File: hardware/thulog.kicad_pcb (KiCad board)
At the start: 2 copper layers, 16 parts, among them IC1 ATTINY2313A-S, K1 DHT, P1 ISP, P2 USB, X1 QUARTZCMS4

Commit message: modified quartz
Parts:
- X1: footprint CONN3_SMD -> SM2512
- moved X1 29.0 mm to (50.8, 31.8), turned to 180 degrees
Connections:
- X1 pad 3: N-000002 -> (no net)
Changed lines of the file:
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@@
 (kicad_pcb (version 3) (host pcbnew "(2013-07-07 BZR 4022)-stable")
   (general
-    (links 34)
-    (no_connects 34)
+    (links 33)
+    (no_connects 33)
     (area 0 0 0 0)
     (thickness 1.6)
@@
     (mod_text_size 1 1)
     (mod_text_width 0.15)
-    (pad_size 1.5 1.5)
-    (pad_drill 0.6)
+    (pad_size 1.99898 2.99974)
+    (pad_drill 0)
     (pad_to_mask_clearance 0)
     (aux_axis_origin 0 0)
@@
     )
   )
-  (module CONN3_SMD (layer F.Cu)
-    (at 25.4 17.78)
-    (attr smd)
-    (fp_text reference X1 (at 0 -0.381) (layer F.SilkS)
-      (effects (font (size 1.016 0.762) (thickness 0.1524)))
-    )
-    (fp_text value QUARTZCMS4 (at 0 -1.524) (layer F.SilkS)
-      (effects (font (size 0.762 0.762) (thickness 0.1524)))
-    )
-    (fp_line (start 2.667 1.3335) (end 2.667 0.381) (layer F.SilkS) (width 0.127))
-    (fp_line (start 2.667 0.381) (end -2.667 0.381) (layer F.SilkS) (width 0.127))
-    (fp_line (start -2.667 0.381) (end -2.667 1.3335) (layer F.SilkS) (width 0.127))
-    (fp_line (start 0 -2.794) (end 2.794 -2.794) (layer F.SilkS) (width 0.127))
-    (fp_line (start 2.794 -2.794) (end 2.794 -2.032) (layer F.SilkS) (width 0.127))
-    (fp_line (start 2.794 -2.032) (end 4.826 -2.032) (layer F.SilkS) (width 0.127))
-    (fp_line (start 4.826 -2.032) (end 4.826 1.3335) (layer F.SilkS) (width 0.127))
-    (fp_line (start 4.826 1.3335) (end -4.826 1.3335) (layer F.SilkS) (width 0.127))
-    (fp_line (start -4.826 1.3335) (end -4.826 -2.032) (layer F.SilkS) (width 0.127))
-    (fp_line (start -4.826 -2.032) (end -2.794 -2.032) (layer F.SilkS) (width 0.127))
-    (fp_line (start -2.794 -2.032) (end -2.794 -2.794) (layer F.SilkS) (width 0.127))
-    (fp_line (start -2.794 -2.794) (end 0 -2.794) (layer F.SilkS) (width 0.127))
-    (pad 3 smd rect (at 1.27 -3.429) (size 0.8128 1.778)
-      (layers F.Cu F.Paste F.Mask)
-      (net 6 N-000002)
-    )
-    (pad 2 smd rect (at 0 -3.429) (size 0.8128 1.778)
-      (layers F.Cu F.Paste F.Mask)
-    )
-    (pad 1 smd rect (at -1.27 -3.429) (size 0.8128 1.778)
-      (layers F.Cu F.Paste F.Mask)
-      (net 2 N-000001)
-    )
-    (pad "" smd rect (at 3.81 -0.4445) (size 2.032 3.048)
-      (layers F.Cu F.Paste F.Mask)
-    )
-    (pad "" smd rect (at -3.81 -0.4445) (size 2.032 3.048)
-      (layers F.Cu F.Paste F.Mask)
-    )
-    (model smd/conn3_smd.wrl
-      (at (xyz 0 0 0))
-      (scale (xyz 0.4 0.4 0.4))
-      (rotate (xyz 0 0 0))
-    )
-  )
   (module SM0805 (layer F.Cu)
     (at 67.31 45.72)
@@
       (rotate (xyz 0 0 0))
     )
+  )
+  (module SM2512 (layer F.Cu)
+    (at 50.8 31.75 180)
+    (tags "CMS SM")
+    (attr smd)
+    (fp_text reference X1 (at -0.8001 0 270) (layer F.SilkS)
+      (effects (font (size 0.889 0.762) (thickness 0.127)))
+    )
+    (fp_text value QUARTZCMS4 (at 0.89916 0 270) (layer F.SilkS)
+      (effects (font (size 0.889 0.762) (thickness 0.127)))
+    )
+    (fp_line (start -3.99956 -2.10058) (end -3.99956 2.10058) (layer F.SilkS) (width 0.14986))
+    (fp_text user + (at -4.59994 2.30124 180) (layer F.SilkS)
+      (effects (font (size 0.7 0.7) (thickness 0.15)))
+    )
+    (fp_line (start -4.30022 -2.10058) (end -4.30022 2.10058) (layer F.SilkS) (width 0.14986))
+    (fp_line (start 4.30022 -2.10058) (end 4.30022 2.10058) (layer F.SilkS) (width 0.14986))
+    (fp_line (start 1.99644 2.10566) (end 4.28244 2.10566) (layer F.SilkS) (width 0.14986))
+    (fp_line (start 4.28244 -2.10566) (end 1.99644 -2.10566) (layer F.SilkS) (width 0.14986))
+    (fp_line (start -1.99898 -2.10566) (end -4.28498 -2.10566) (layer F.SilkS) (width 0.14986))
+    (fp_line (start -4.28244 2.10566) (end -1.99644 2.10566) (layer F.SilkS) (width 0.14986))
+    (pad 1 smd rect (at -2.99974 0 180) (size 1.99898 2.99974)
+      (layers F.Cu F.Paste F.Mask)
+      (net 2 N-000001)
+    )
+    (pad 3 smd rect (at 2.99974 0 180) (size 1.99898 2.99974)
+      (layers F.Cu F.Paste F.Mask)
+    )
+    (model smd\chip_smd_pol_wide.wrl
+      (at (xyz 0 0 0))
+      (scale (xyz 0.35 0.35 0.35))
+      (rotate (xyz 0 0 0))
+    )

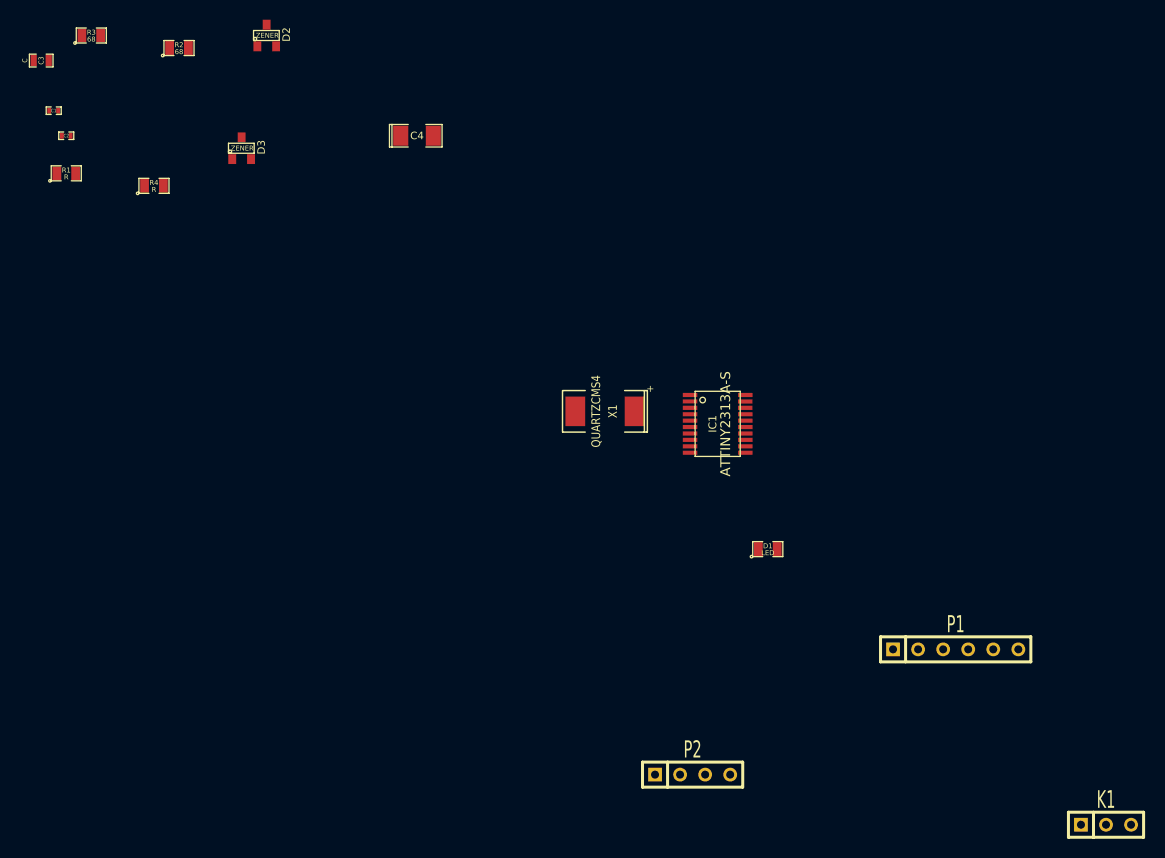
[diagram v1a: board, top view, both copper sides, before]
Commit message: drawing the pcb
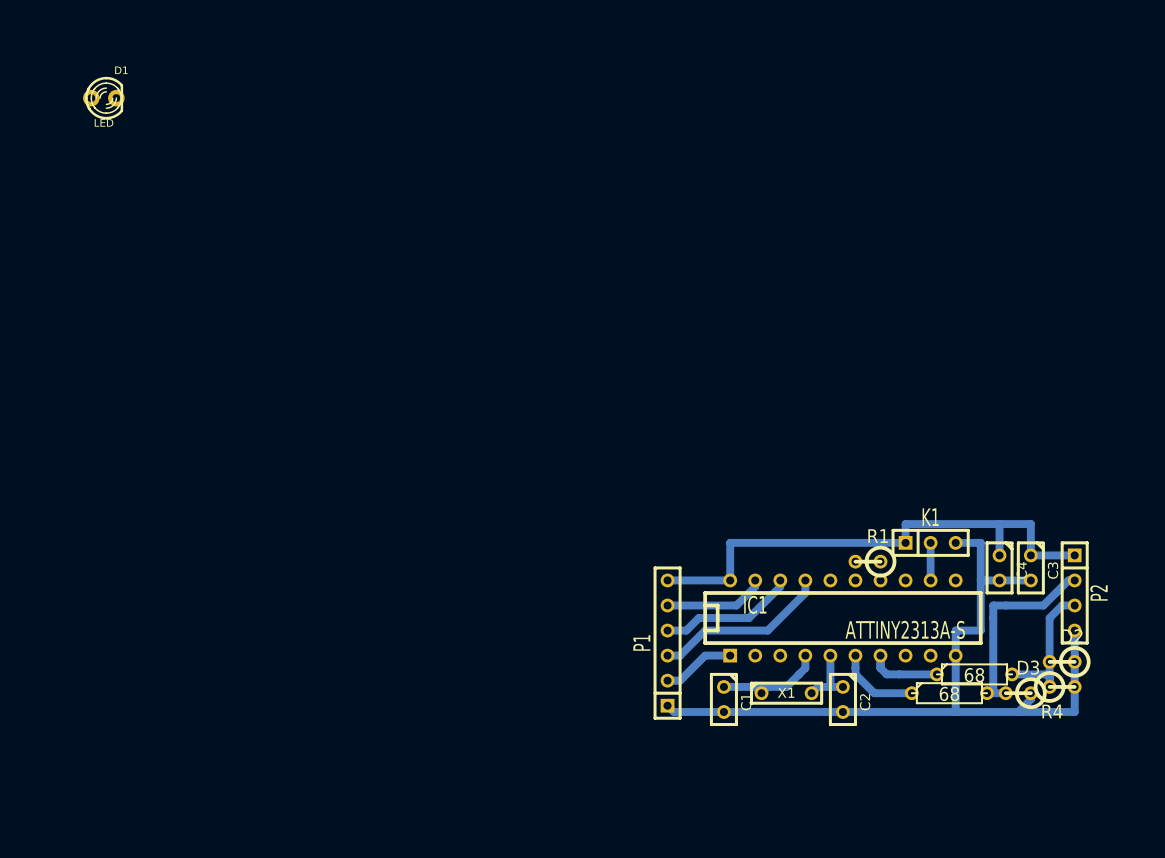
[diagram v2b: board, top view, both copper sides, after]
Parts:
- C1, C2: footprint SM0402_c -> C1
- C3: footprint SM0603_Capa -> C1
- C4: footprint SM1206POL -> C1
- D1: footprint SM0805 -> LED-3MM
- D2, D3: footprint SOT23 -> R1
- IC1: footprint tssop-20 -> DIP-20__300
- R1, R4: footprint SM0805 -> R1
- R2, R3: footprint SM0805 -> R3
- X1: footprint SM2512 -> C2
- moved C3 112.7 mm to (94.0, 47.6), turned to 270 degrees
- moved R3 110.5 mm to (88.3, 58.4)
- moved R4 105.2 mm to (97.2, 59.7)
- moved D2 102.6 mm to (97.2, 57.1), turned to 180 degrees
- moved R2 101.9 mm to (85.7, 60.3)
- moved C2 97.3 mm to (74.9, 61.0), turned to 270 degrees
- moved D3 96.2 mm to (92.7, 60.3), turned to 180 degrees
- moved C1 90.4 mm to (62.9, 61.0), turned to 270 degrees
- moved R1 90.3 mm to (77.5, 47.0), turned to 180 degrees
- moved D1 81.4 mm to (0.00, 0.00)
- moved C4 73.5 mm to (90.8, 47.6), turned to 270 degrees
- moved P2 42.9 mm to (98.4, 50.2), turned to 270 degrees
- moved X1 34.0 mm to (69.2, 60.3), turned to 0 degrees
- moved K1 33.7 mm to (83.8, 45.1)
- moved P1 29.2 mm to (57.1, 55.2), turned to 90 degrees
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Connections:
- C2 pad 1: N-000002 -> N-000009
- IC1 pad 13: (no net) -> N-0000010
- IC1 pad 5: N-000002 -> N-000009
- IC1 pad 8: N-0000023 (its old number) -> (no net)
- P1 pad 1: VCC -> GND
- P1 pad 6: GND -> VCC
- R1 pad 1: N-0000023 (its old number) -> N-0000010
- X1 pad 3: (no net) -> N-000009
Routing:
- net GND: track 0.00 -> 79.5 mm
- net VCC: track 0.00 -> 53.3 mm
- net N-0000022: track 0.00 -> 20.7 mm
- net N-000001: track 0.00 -> 17.9 mm
- net N-0000023: track 0.00 -> 15.1 mm
- net N-000004: track 0.00 -> 13.9 mm
- net N-000008: track 0.00 -> 12.1 mm
- net N-000003: track 0.00 -> 10.3 mm
- net N-0000018: track 0.00 -> 8.52 mm
- net N-0000019: track 0.00 -> 8.41 mm
- net RESET: track 0.00 -> 7.40 mm
- net N-000009: track 0.00 -> 6.61 mm
- net N-000006: track 0.00 -> 3.81 mm
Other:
- net class Default: trace_width 0.254 -> 0.8

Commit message: finished with pcb, ready to be printed
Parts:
- added P3: CONN_2, SIL-2, B.Cu at (132.3, 64.0)
- C1, C2, C3, C4: footprint C1 -> SM0805
- D2, D3, R1, R4: footprint R1 -> SM0805
- IC1: footprint DIP-20__300 -> SO20L
- K1, P1, X1: moved to B.Cu
- P2: value USB -> CONN_2; footprint SIL-4 -> SIL-2; moved to B.Cu
- R2, R3: footprint R3 -> SM0805
- moved D1 125.1 mm to (118.6, 39.9), turned to 220 degrees
- moved C1 71.9 mm to (134.1, 51.1), turned to 0 degrees
- moved P1 70.3 mm to (127.3, 60.7), turned to 180 degrees
- moved X1 64.4 mm to (132.8, 50.3), turned to 90 degrees
- moved C2 60.9 mm to (134.1, 46.7), turned to 0 degrees
- moved R2 53.6 mm to (139.2, 56.6), turned to 270 degrees
- moved IC1 51.1 mm to (125.7, 47.0), turned to 90 degrees
- moved R3 49.0 mm to (136.9, 52.6), turned to 270 degrees
- moved D3 46.1 mm to (138.7, 64.0), turned to 0 degrees
- moved P2 41.4 mm to (138.4, 60.7), turned to 180 degrees
- moved R1 40.1 mm to (117.6, 48.0), turned to 270 degrees
- moved R4 38.9 mm to (135.9, 55.6), turned to 180 degrees
- moved D2 38.7 mm to (135.9, 57.7), turned to 0 degrees
- moved C4 34.4 mm to (120.9, 64.3)
- moved K1 31.1 mm to (108.5, 64.0), turned to 180 degrees
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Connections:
- D1 pad 1: N-0000011 -> N-0000010
- D1 pad 2: GND -> N-000007
- IC1 pad 7: N-0000018 -> (no net)
- IC1 pad 8: (no net) -> N-000008
- P2 pad 1: VCC -> N-0000022
- P2 pad 2: N-0000022 -> N-0000023
- R1 pad 1: N-0000010 -> N-000007
- R1 pad 2: N-0000011 -> GND
- R3 pad 1: N-0000018 -> N-000008
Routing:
- net N-0000017: track 8.41 -> 38.5 mm
- net N-000002: track 3.81 -> 33.7 mm
- net N-000008: track 0.00 -> 26.2 mm
- net N-0000022: track 20.7 -> 6.65 mm
- net GND: track 79.5 -> 91.7 mm
- net N-0000010: track 0.00 -> 10.6 mm
- net N-0000018: track 8.52 -> 0.00 mm
- net N-0000023: track 15.1 -> 7.33 mm
- net N-000007: track 0.00 -> 6.38 mm
- net N-0000013: track 12.1 -> 6.45 mm
- net N-0000014: track 6.61 -> 2.15 mm
- net VCC: track 53.3 -> 55.7 mm
- net N-000006: track 17.9 -> 16.1 mm
- net N-000004: track 10.3 -> 11.1 mm
- net RESET: track 7.40 -> 8.08 mm
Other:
- board outline added: 37.6 x 30.7 mm
- net class Default: trace_width 0.8 -> 0.5

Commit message: adjusted the pbc
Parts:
- moved K1 0.51 mm to (109.0, 64.0)
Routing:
- net VCC: track 55.7 -> 42.2 mm
- net N-000006: track 16.1 -> 19.2 mm
- net N-000005: track 13.6 -> 15.4 mm
- net GND: track 91.7 -> 90.7 mm
- net N-000004: track 11.1 -> 11.7 mm
- net N-000002: track 33.7 -> 33.2 mm
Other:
- board size 37.6 x 30.7 mm -> 37.8 x 30.7 mm

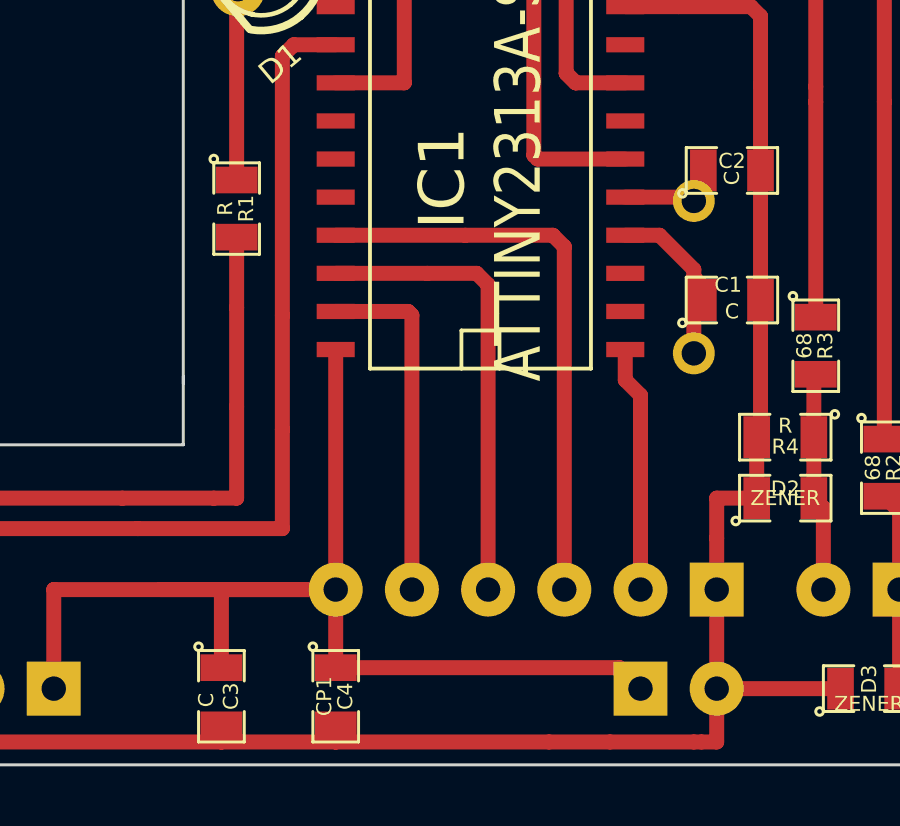
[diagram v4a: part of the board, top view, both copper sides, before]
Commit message: adjusted 0.1uF cap
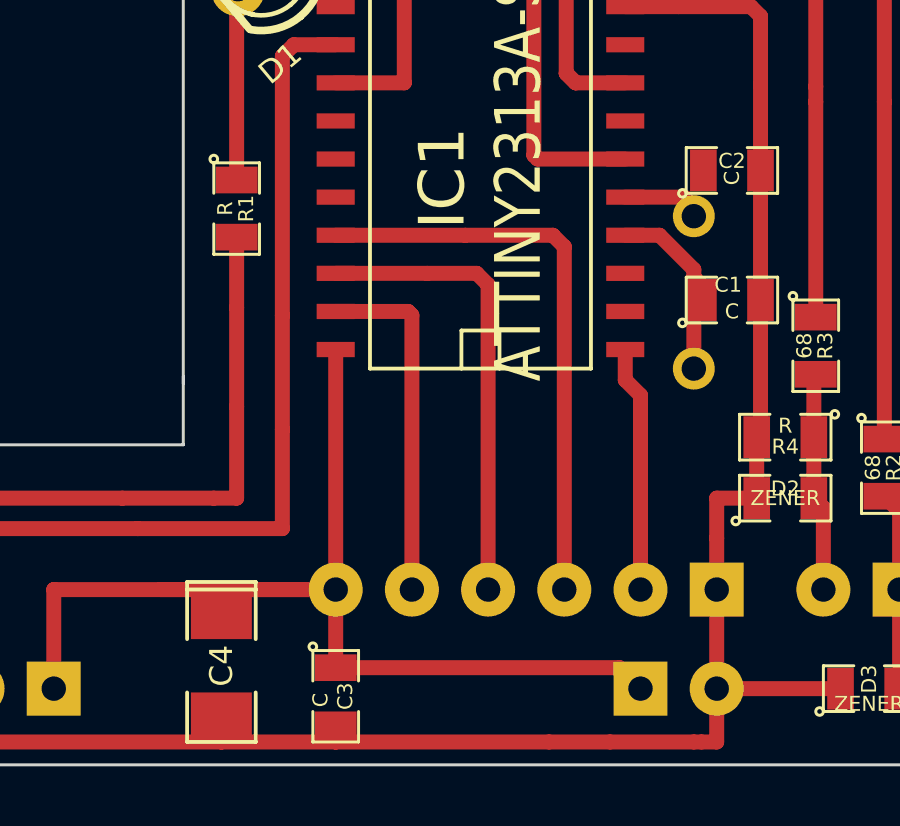
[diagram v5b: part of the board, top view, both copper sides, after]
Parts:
- C4: footprint SM0805 -> SM1206POL
- moved C4 3.94 mm to (117.1, 63.2)
- moved C3 3.81 mm to (120.9, 64.3)
- moved X1 0.51 mm to (132.8, 50.8)
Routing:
- net VCC: track 42.2 -> 40.7 mm
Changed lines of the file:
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@@
     (links 34)
     (no_connects 1)
-    (area 103.078001 35.763999 163.448 76.614)
+    (area 103.327999 35.763999 163.448 67.81927)
     (thickness 1.6)
     (drawings 9)
@@
   )
   (module C2 (layer B.Cu)
-    (at 132.842 50.292 90)
+    (at 132.842 50.8 90)
     (descr "Condensateur = 2 pas")
     (tags C)
@@
   (module SM0805 (layer F.Cu)
     (at 120.904 64.262 270)
-    (attr smd)
-    (fp_text reference C4 (at 0 -0.3175 270) (layer F.SilkS)
-      (effects (font (size 0.50038 0.50038) (thickness 0.10922)))
-    )
-    (fp_text value CP1 (at 0 0.381 270) (layer F.SilkS)
-      (effects (font (size 0.50038 0.50038) (thickness 0.10922)))
-    )
-    (fp_circle (center -1.651 0.762) (end -1.651 0.635) (layer F.SilkS) (width 0.09906))
-    (fp_line (start -0.508 0.762) (end -1.524 0.762) (layer F.SilkS) (width 0.09906))
-    (fp_line (start -1.524 0.762) (end -1.524 -0.762) (layer F.SilkS) (width 0.09906))
-    (fp_line (start -1.524 -0.762) (end -0.508 -0.762) (layer F.SilkS) (width 0.09906))
-    (fp_line (start 0.508 -0.762) (end 1.524 -0.762) (layer F.SilkS) (width 0.09906))
-    (fp_line (start 1.524 -0.762) (end 1.524 0.762) (layer F.SilkS) (width 0.09906))
-    (fp_line (start 1.524 0.762) (end 0.508 0.762) (layer F.SilkS) (width 0.09906))
-    (pad 1 smd rect (at -0.9525 0 270) (size 0.889 1.397)
-      (layers F.Cu F.Paste F.Mask)
-      (net 15 VCC)
-    )
-    (pad 2 smd rect (at 0.9525 0 270) (size 0.889 1.397)
-      (layers F.Cu F.Paste F.Mask)
-      (net 1 GND)
-    )
-    (model smd/chip_cms.wrl
-      (at (xyz 0 0 0))
-      (scale (xyz 0.1 0.1 0.1))
-      (rotate (xyz 0 0 0))
-    )
-  )
-  (module SM0805 (layer F.Cu)
-    (at 117.094 64.262 270)
     (attr smd)
     (fp_text reference C3 (at 0 -0.3175 270) (layer F.SilkS)
@@
     )
   )
-  (gr_line (start 103.632 66.548) (end 103.378 66.548) (angle 90) (layer Edge.Cuts) (width 0.1))
-  (gr_line (start 103.632 55.88) (end 103.632 66.548) (angle 90) (layer Edge.Cuts) (width 0.1))
-  (gr_line (start 115.824 55.88) (end 115.824 53.594) (angle 90) (layer Edge.Cuts) (width 0.1))
-  (gr_line (start 103.632 55.88) (end 115.824 55.88) (angle 90) (layer Edge.Cuts) (width 0.1))
+  (module SM1206POL (layer F.Cu)
+    (at 117.094 63.246 270)
+    (attr smd)
+    (fp_text reference C4 (at 0 0 270) (layer F.SilkS)
+      (effects (font (size 0.762 0.762) (thickness 0.127)))
+    )
+    (fp_text value CP1 (at 0 0 270) (layer F.SilkS) hide
+      (effects (font (size 0.762 0.762) (thickness 0.127)))
+    )
+    (fp_line (start -2.54 -1.143) (end -2.794 -1.143) (layer F.SilkS) (width 0.127))
+    (fp_line (start -2.794 -1.143) (end -2.794 1.143) (layer F.SilkS) (width 0.127))
+    (fp_line (start -2.794 1.143) (end -2.54 1.143) (layer F.SilkS) (width 0.127))
+    (fp_line (start -2.54 -1.143) (end -2.54 1.143) (layer F.SilkS) (width 0.127))
+    (fp_line (start -2.54 1.143) (end -0.889 1.143) (layer F.SilkS) (width 0.127))
+    (fp_line (start 0.889 -1.143) (end 2.54 -1.143) (layer F.SilkS) (width 0.127))
+    (fp_line (start 2.54 -1.143) (end 2.54 1.143) (layer F.SilkS) (width 0.127))
+    (fp_line (start 2.54 1.143) (end 0.889 1.143) (layer F.SilkS) (width 0.127))
+    (fp_line (start -0.889 -1.143) (end -2.54 -1.143) (layer F.SilkS) (width 0.127))
+    (pad 1 smd rect (at -1.651 0 270) (size 1.524 2.032)
+      (layers F.Cu F.Paste F.Mask)
+      (net 15 VCC)
+    )
+    (pad 2 smd rect (at 1.651 0 270) (size 1.524 2.032)
+      (layers F.Cu F.Paste F.Mask)
+      (net 1 GND)
+    )
+    (model smd/chip_cms_pol.wrl
+      (at (xyz 0 0 0))
+      (scale (xyz 0.17 0.16 0.16))
+      (rotate (xyz 0 0 0))
+    )
+  )
   (dimension 30.734 (width 0.3) (layer Eco2.User)
-    (gr_text "30.734 mm" (at 156.798 51.181 90) (layer Eco2.User)
+    (gr_text "30.734 mm" (at 156.798 51.181 270) (layer Eco2.User)
       (effects (font (size 1.5 1.5) (thickness 0.3)))
     )
@@
     (arrow2b (pts (xy 155.448 66.548) (xy 154.86158 65.421497)))
   )
+  (gr_line (start 103.632 66.548) (end 103.378 66.548) (angle 90) (layer Edge.Cuts) (width 0.1))
+  (gr_line (start 103.632 55.88) (end 103.632 66.548) (angle 90) (layer Edge.Cuts) (width 0.1))
+  (gr_line (start 115.824 55.88) (end 115.824 53.594) (angle 90) (layer Edge.Cuts) (width 0.1))
+  (gr_line (start 103.632 55.88) (end 115.824 55.88) (angle 90) (layer Edge.Cuts) (width 0.1))
   (gr_line (start 141.224 66.548) (end 103.632 66.548) (angle 90) (layer Edge.Cuts) (width 0.1))
   (gr_line (start 141.224 35.814) (end 141.224 66.548) (angle 90) (layer Edge.Cuts) (width 0.1))
   (gr_line (start 115.824 35.814) (end 141.224 35.814) (angle 90) (layer Edge.Cuts) (width 0.1))
   (gr_line (start 115.824 53.848) (end 115.824 35.814) (angle 90) (layer Edge.Cuts) (width 0.1))
-  (segment (start 106.426 65.786) (end 106.426 64.008) (width 0.5) (layer F.Cu) (net 1) (status 800000))
-  (segment (start 106.426 64.008) (end 106.426 57.658) (width 0.5) (layer F.Cu) (net 1) (status 400000))
+  (segment (start 106.426 65.786) (end 106.426 64.008) (width 0.5) (layer F.Cu) (net 1))
+  (segment (start 106.426 64.008) (end 106.426 57.658) (width 0.5) (layer F.Cu) (net 1))
   (segment (start 117.094 65.2145) (end 117.094 65.786) (width 0.5) (layer F.Cu) (net 1))
   (segment (start 120.904 65.2145) (end 120.904 65.786) (width 0.5) (layer F.Cu) (net 1))
@@
   (segment (start 127.508 39.08425) (end 134.62 39.08425) (width 0.5) (layer F.Cu) (net 5))
   (segment (start 127.635 46.355) (end 130.556 46.355) (width 0.5) (layer F.Cu) (net 5))
-  (segment (start 108.966 64.008) (end 108.966 58.674) (width 0.5) (layer F.Cu) (net 6) (status 400000))
+  (segment (start 108.966 64.008) (end 108.966 58.674) (width 0.5) (layer F.Cu) (net 6))
   (segment (start 119.126 42.926) (end 119.507 42.545) (width 0.5) (layer F.Cu) (net 6))
   (segment (start 119.126 51.562) (end 119.126 42.926) (width 0.5) (layer F.Cu) (net 6))
@@
   (segment (start 130.556 53.721) (end 130.556 52.705) (width 0.5) (layer F.Cu) (net 14))
   (segment (start 131.064 54.229) (end 130.556 53.721) (width 0.5) (layer F.Cu) (net 14))
-  (segment (start 111.506 64.008) (end 111.506 60.706) (width 0.5) (layer F.Cu) (net 15) (status 400000))
+  (segment (start 117.094 61.849) (end 117.094 60.706) (width 0.5) (layer F.Cu) (net 15))
+  (segment (start 111.506 64.008) (end 111.506 60.706) (width 0.5) (layer F.Cu) (net 15))
   (segment (start 111.506 60.706) (end 120.904 60.706) (width 0.5) (layer F.Cu) (net 15))
-  (segment (start 117.094 63.3095) (end 117.094 60.706) (width 0.5) (layer F.Cu) (net 15))
   (segment (start 120.904 63.3095) (end 130.3655 63.3095) (width 0.5) (layer F.Cu) (net 15))
   (segment (start 130.3655 63.3095) (end 131.064 64.008) (width 0.5) (layer F.Cu) (net 15))
